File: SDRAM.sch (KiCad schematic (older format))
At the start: 48 parts, among them U3 MT41K512M16HA-125_E, U31 TPS51200DRC

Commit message: DDR terminations changed, HTML BoM with variant added
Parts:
- removed C14, C15, C16, C17, C18, C19, C20, C21, C23, C25: 100nF, Capacitors SMD:CAPC0603X33N, symbol AMC_FMC_Carrier-PcbDoc-rescue:C-Device
- removed C22, C26, C27: 22uF, Capacitors SMD:CAPC1709X100N, symbol AMC_FMC_Carrier-PcbDoc-rescue:C-Device
- removed C24: 1uF, Capacitors SMD:CAPC1005X55N, symbol AMC_FMC_Carrier-PcbDoc-rescue:C-Device
- removed R10, R106, R11, R12, R13, R14, R15, R16, R17, R18, R19, R20, R21, R22, R23, R27, R4, R5, R6, R7, R8, R9: R0402_51R_1%_0.0625W_100PPM, RESC1005X40N, symbol Resistors_SMD:R0402_51R_1%_0.0625W_100PPM
- added C14, C15, C16, C17, C18, C19, C20, C21, C23, C25, C365, C366, C367, C368, C369: CC0201_100NF_6.3V_10%_X5R, CAPC0603X33N, symbol Capacitors_SMD:CC0201_100NF_6.3V_10%_X5R
- added C22, C26, C27: CC0603_22UF_6.3V_20%_X5R, CAPC1709X100N, symbol Capacitors_SMD:CC0603_22UF_6.3V_20%_X5R
- added C24: CC0402_1UF_16V_10%_X5R, CAPC1005X55N, symbol Capacitors_SMD:CC0402_1UF_16V_10%_X5R
- added R10, R106, R11, R12, R13, R14, R15, R16, R17, R18, R19, R20, R21, R22, R23, R27, R4, R5, R6, R7, R8, R9: R0402_40R2_1%_0.0625W_100PPM, RESC1005X40N, symbol Resistors_SMD:R0402_40R2_1%_0.0625W_100PPM
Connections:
- wire segments 223 -> 231

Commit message: SW2 placement changed, BOM cleared, FPGA boot, less ERC errors and wornings
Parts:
- added C364, C373: CC0603_4.7UF_16V_10%_X5R, CAPC1709X95N, symbol Capacitors_SMD:CC0603_4.7UF_16V_10%_X5R
- added C370, C371, C372: CC0201_100NF_6.3V_10%_X5R, CAPC0603X33N, symbol Capacitors_SMD:CC0201_100NF_6.3V_10%_X5R
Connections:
- wire segments 231 -> 241

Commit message: BOM updated, 25MHz clock level fixed
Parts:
- U31: symbol AMC_FMC_Carrier-PcbDoc-rescue:TPS51200DRC-Regulator_Linear -> AMC_FMC_Carrier-PcbDoc-rescue:TPS51200DRC-Regulator_Linear-AMC_FMC_Carrier-PcbDoc-rescue
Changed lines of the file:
@@
 	2950 3250 4800 3250
 $Comp
-L AMC_FMC_Carrier-PcbDoc-rescue:VTT_DDR3-powerMG #PWR0225
+L AMC_FMC_Carrier-PcbDoc-rescue:VTT_DDR3-powerMG-AMC_FMC_Carrier-PcbDoc-rescue #PWR0225
 U 1 1 5D9E969E
 P 3300 2750
@@
 $EndComp
 $Comp
-L AMC_FMC_Carrier-PcbDoc-rescue:VTT_DDR3-powerMG #PWR0224
+L AMC_FMC_Carrier-PcbDoc-rescue:VTT_DDR3-powerMG-AMC_FMC_Carrier-PcbDoc-rescue #PWR0224
 U 1 1 5DA46618
 P 2550 1050
@@
 Connection ~ 2550 1050
 $Comp
-L AMC_FMC_Carrier-PcbDoc-rescue:VTT_DDR3-powerMG #PWR0457
+L AMC_FMC_Carrier-PcbDoc-rescue:VTT_DDR3-powerMG-AMC_FMC_Carrier-PcbDoc-rescue #PWR0457
 U 1 1 5DA7582E
 P 10800 5200
@@
 	10400 5200 10800 5200
 $Comp
-L AMC_FMC_Carrier-PcbDoc-rescue:TPS51200DRC-Regulator_Linear U31
+L AMC_FMC_Carrier-PcbDoc-rescue:TPS51200DRC-Regulator_Linear-AMC_FMC_Carrier-PcbDoc-rescue U31
 U 1 1 5BDAE091
 P 8150 5400
@@
 $EndComp
 $Comp
-L AMC_FMC_Carrier-PcbDoc-rescue:VTT_DDR3-powerMG #PWR0653
+L AMC_FMC_Carrier-PcbDoc-rescue:VTT_DDR3-powerMG-AMC_FMC_Carrier-PcbDoc-rescue #PWR0653
 U 1 1 5CDF4563
 P 950 7250

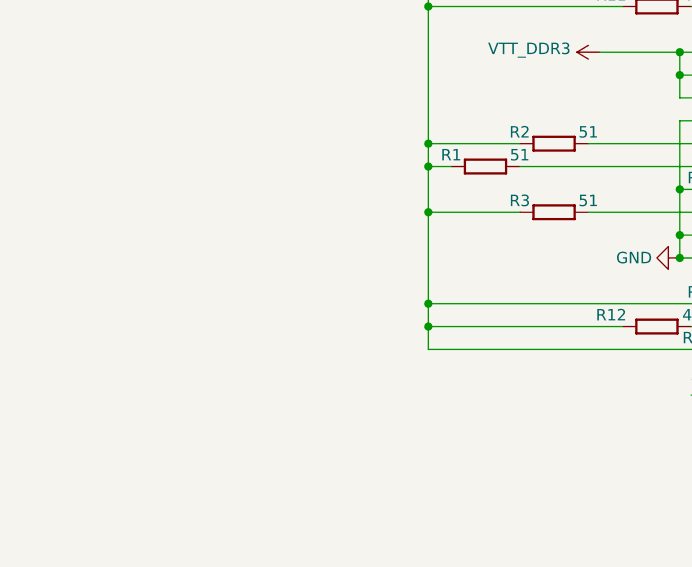
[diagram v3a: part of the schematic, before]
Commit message: U.FL for clock, logos moved, MII -> RGMII, new symbol library, git tag added
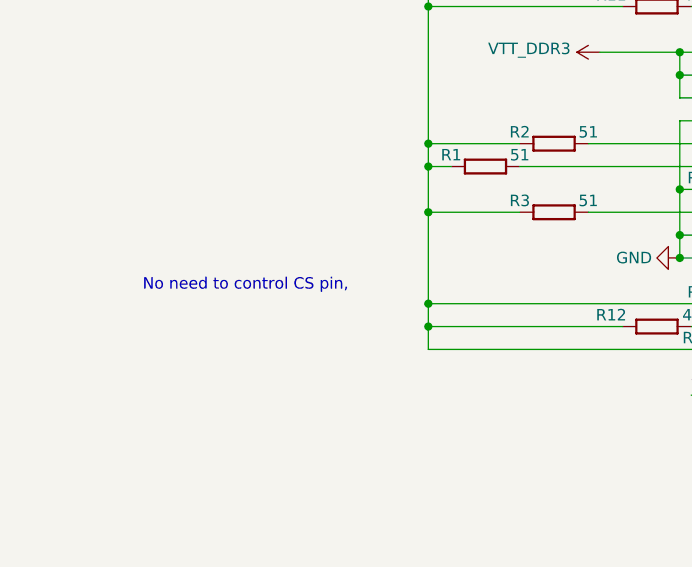
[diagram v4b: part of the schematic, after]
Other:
- note added: "No need to control CS pin,"
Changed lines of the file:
@@
 Wire Bus Line
 	10150 1150 10150 2750
+Text Notes 1300 3800 0    50   ~ 0
+No need to control CS pin,
 $EndSCHEMATC

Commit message: BOM configuration file edited, updated Marble picture, some components part number changed
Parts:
- U3: symbol Logic:MT41K512M16HA-125_E -> AMC_FMC_Carrier-PcbDoc-rescue:MT41K512M16HA-125_E-Logic; Manufacturer Part Number MT41K512M16HA-125:E -> MT41K512M16HA-125:E (AS4C512M16D3L-12BCN)
- U31: Manufacturer Part Number (none) -> TPS51200DRC
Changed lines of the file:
@@
 Connection ~ 3650 2850
 $Comp
-L Logic:MT41K512M16HA-125_E U3
+L AMC_FMC_Carrier-PcbDoc-rescue:MT41K512M16HA-125_E-Logic U3
 U 1 1 5C4F8488
 P 5000 950
@@
 F 13 "+1.35V, 8Gb (64 Meg x 16 x 8 banks) DDR3L SDRAM" H 5000 -6210 60  0001 L CNN "Part Description"
 F 14 "MICRON TECHNOLOGY" H 5000 -6300 60  0001 L CNN "Manufacturer"
-F 15 "MT41K512M16HA-125:E" H 5000 -6390 60  0001 L CNN "Manufacturer Part Number"
+F 15 "MT41K512M16HA-125:E (AS4C512M16D3L-12BCN)" H 5000 -6390 60  0001 L CNN "Manufacturer Part Number"
 F 16 "96" H 5000 -6480 60  0001 L CNN "Pin Count"
 F 17 "BGA96" H 5000 -6570 60  0001 L CNN "Case"
@@
 F 2 "ICs_And_Semiconductors_SMD:TEXAS_DRC (S-PVSON-N10)" H 8150 6250 50  0001 C CNN
 F 3 "http://www.ti.com/lit/ds/symlink/tps51200.pdf" H 8150 6250 50  0001 C CNN
+F 4 "TPS51200DRC" H 8150 5400 50  0001 C CNN "Manufacturer Part Number"
 	1    8150 5400
 	1    0    0    -1

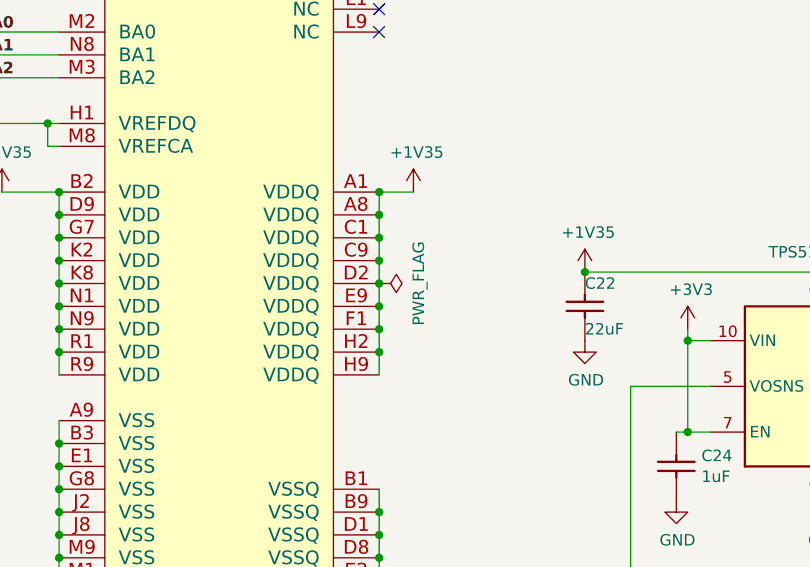
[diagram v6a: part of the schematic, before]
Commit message: README edited, less ERC errors and warnings
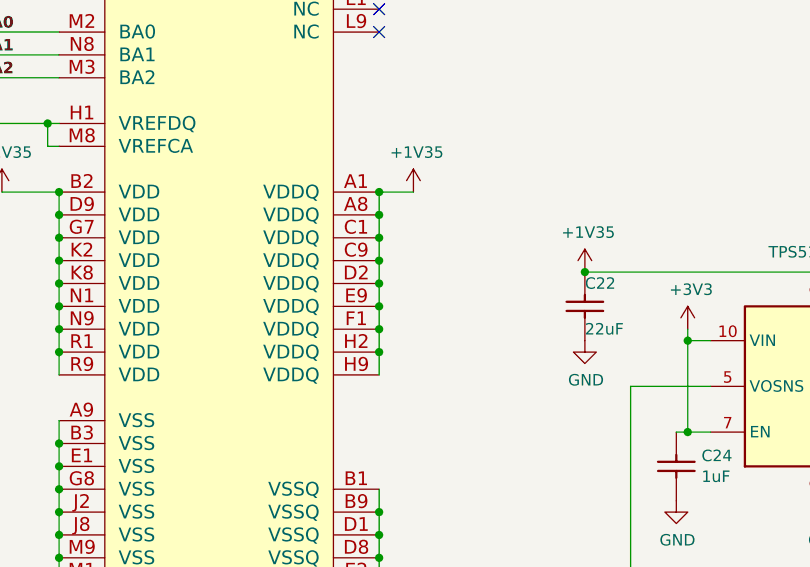
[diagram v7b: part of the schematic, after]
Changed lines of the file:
@@
-$EndComp
-$Comp
-L power:PWR_FLAG #FLG?
-U 1 1 5D7ED8A7
-P 6200 4950
-AR Path="/5BABAC65/5D7ED8A7" Ref="#FLG?"  Part="1"
-AR Path="/5BD32060/5D7ED8A7" Ref="#FLG0146"  Part="1"
-F 0 "#FLG0146" H 6200 5025 50  0001 C CNN
-F 1 "PWR_FLAG" H 6200 5123 50  0000 C CNN
-F 2 "" H 6200 4950 50  0001 C CNN
-F 3 "~" H 6200 4950 50  0001 C CNN
-	1    6200 4950
-	0    1    1    0
 $EndComp
 $Comp
